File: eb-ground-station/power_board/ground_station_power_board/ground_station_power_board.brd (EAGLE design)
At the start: 125 x 78 mm, 70 parts, among them J1 CONN_20X2SHROUDED, Q1 SQJ459EP_MOSFET_P_CHAN, Q15 DMN61D8LVT-DUAL-N-CHANNEL-MOS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, Q17 DMN61D8LVT-DUAL-N-CHANNEL-MOS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, Q18 DMN61D8LVT-DUAL-N-CHANNEL-MOS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, Q2 SQJ459EP_MOSFET_P_CHAN, Q22 TC4427-FET-GATE-DRVR, Q23 TC4427-FET-GATE-DRVR, Q24 TC4427-FET-GATE-DRVR, Q3 SQJ459EP_MOSFET_P_CHAN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

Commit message: every time I look at this I add 40 more vias
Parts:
- added J2: (no value), SparkFun-Connectors:1X01NS_KIT
- added R14: 4.7k, SparkFun-Resistors:0603
- added U$8: (no value), Oliver_Custom:PSAS_LOGO_15X15
- R10, R8, R9: value EXB-A10P391JC_ARRAY_EXBA-M -> 10k
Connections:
- new net N$6: J2.1, R14.1, U2.14
- net 3.3V: now also R14.2
- net GND: no longer U2.14
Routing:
- net N$6: track 0.00 -> 13.9 mm, vias 0 -> 2
- net 3.3V: track 106.5 -> 108.6 mm
- net GND: vias 297 -> 314
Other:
- board text added: "!RESET->"
- board text added: "1.5A MAX"
- board text added: "10A MAX"
- board text added: "30A MAX"
- board text added: "500mA MAX"
- board text added: "ORESAT GROUND STATION POWER BOARD OLIVER REW 2018-07-31"
- board text removed: "ORESAT GROUND STATION POWER BOARD OLIVER REW 2018-07-29"

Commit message: added decoupling cap and some labels
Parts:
- added C11: 0.1uF, SparkFun-Capacitors:0603
- moved D5 3.00 mm to (12.9, 62.1)
- moved R3 3.00 mm to (12.9, 60.0)
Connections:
- net 3.3V: now also C11.1
- net GND: now also C11.2
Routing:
- net 3.3V: track 108.6 -> 109.9 mm
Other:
- board text added: "LOWER"
- board text added: "UPPER"
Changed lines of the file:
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@@
 <layer number="22" name="bPlace" color="7" fill="1" visible="yes" active="yes"/>
 <layer number="23" name="tOrigins" color="15" fill="1" visible="yes" active="yes"/>
-<layer number="24" name="bOrigins" color="15" fill="1" visible="yes" active="yes"/>
+<layer number="24" name="bOrigins" color="15" fill="1" visible="no" active="yes"/>
 <layer number="25" name="tNames" color="7" fill="1" visible="yes" active="yes"/>
 <layer number="26" name="bNames" color="7" fill="1" visible="yes" active="yes"/>
@@
 <text x="73" y="75" size="1.2" layer="21" ratio="15" rot="SR0">ADC-IN</text>
 <text x="75" y="57" size="1.2" layer="21" ratio="15" rot="SR0">GROUND</text>
-<wire x1="23.36" y1="61.05" x2="18.36" y2="61.05" width="0.5" layer="21"/>
-<wire x1="18.36" y1="61.05" x2="13.36" y2="61.05" width="0.5" layer="21"/>
-<wire x1="13.36" y1="61.05" x2="13.36" y2="66.05" width="0.5" layer="21"/>
-<wire x1="13.36" y1="66.05" x2="18.36" y2="66.05" width="0.5" layer="21"/>
-<wire x1="18.36" y1="66.05" x2="23.36" y2="66.05" width="0.5" layer="21"/>
-<wire x1="23.36" y1="66.05" x2="23.36" y2="61.05" width="0.5" layer="21"/>
-<wire x1="18.36" y1="66.05" x2="18.36" y2="61.05" width="0.5" layer="21"/>
-<text x="14.09" y="62.775" size="1.5" layer="21" ratio="15" rot="SR0">12V</text>
-<text x="18.945" y="62.775" size="1.5" layer="21" ratio="15" rot="SR0">GND</text>
+<wire x1="20.36" y1="61.05" x2="15.36" y2="61.05" width="0.5" layer="21"/>
+<wire x1="15.36" y1="61.05" x2="10.36" y2="61.05" width="0.5" layer="21"/>
+<wire x1="10.36" y1="61.05" x2="10.36" y2="66.05" width="0.5" layer="21"/>
+<wire x1="10.36" y1="66.05" x2="15.36" y2="66.05" width="0.5" layer="21"/>
+<wire x1="15.36" y1="66.05" x2="20.36" y2="66.05" width="0.5" layer="21"/>
+<wire x1="20.36" y1="66.05" x2="20.36" y2="61.05" width="0.5" layer="21"/>
+<wire x1="15.36" y1="66.05" x2="15.36" y2="61.05" width="0.5" layer="21"/>
+<text x="11.09" y="62.775" size="1.5" layer="21" ratio="15" rot="SR0">12V</text>
+<text x="15.945" y="62.775" size="1.5" layer="21" ratio="15" rot="SR0">GND</text>
 <text x="24.5" y="70.75" size="0.8128" layer="21" ratio="15" rot="SR0">A1</text>
 <text x="29.5" y="70.75" size="0.8128" layer="21" ratio="15" rot="SR0">A0</text>
@@
 <text x="55.375" y="72.75" size="1" layer="21" ratio="15" rot="SR0">500mA MAX</text>
 <text x="38.25" y="59.125" size="1" layer="21" ratio="15" rot="SR0">1.5A MAX</text>
-<text x="15.5" y="66.625" size="1" layer="21" ratio="15" rot="SR0">30A MAX</text>
+<text x="12.5" y="66.625" size="1" layer="21" ratio="15" rot="SR0">30A MAX</text>
 <text x="58.375" y="59.25" size="1" layer="21" ratio="15" rot="SR0">500mA MAX</text>
+<text x="26.375" y="61.25" size="1" layer="21" ratio="15" rot="SR90">LOWER</text>
+<text x="23.375" y="67.25" size="1" layer="21" ratio="15" rot="SR90">UPPER</text>
 </plain>
 <attributes>
@@
 <attribute name="VALUE" x="39.5" y="62.635" size="0.6096" layer="27" font="vector" ratio="20" rot="R180" align="top-center"/>
 </element>
-<element name="D5" library="SparkFun-LED" package="LED-0603" value="" x="15.86" y="62.065" smashed="yes">
-<attribute name="NAME" x="12.485" y="62.305" size="0.6096" layer="25" font="vector" ratio="15" rot="R180" align="bottom-center"/>
-<attribute name="VALUE" x="15.86" y="61.43" size="0.6096" layer="27" font="vector" ratio="20" align="top-center"/>
-</element>
-<element name="R3" library="SparkFun-Resistors" package="0603" value="806" x="15.89" y="59.995" smashed="yes" rot="R180">
-<attribute name="NAME" x="13.515" y="60.233" size="0.6096" layer="25" font="vector" ratio="15" rot="R180" align="bottom-center"/>
-<attribute name="PROD_ID" value="RES-07857" x="15.89" y="59.995" size="1.778" layer="27" rot="R180" display="off"/>
-<attribute name="VALUE" x="15.89" y="60.757" size="0.6096" layer="27" font="vector" ratio="20" rot="R180" align="top-center"/>
+<element name="D5" library="SparkFun-LED" package="LED-0603" value="" x="12.86" y="62.065" smashed="yes">
+<attribute name="NAME" x="9.485" y="62.305" size="0.6096" layer="25" font="vector" ratio="15" rot="R180" align="bottom-center"/>
+<attribute name="VALUE" x="12.86" y="61.43" size="0.6096" layer="27" font="vector" ratio="20" align="top-center"/>
+</element>
+<element name="R3" library="SparkFun-Resistors" package="0603" value="806" x="12.89" y="59.995" smashed="yes" rot="R180">
+<attribute name="NAME" x="10.515" y="60.233" size="0.6096" layer="25" font="vector" ratio="15" rot="R180" align="bottom-center"/>
+<attribute name="PROD_ID" value="RES-07857" x="12.89" y="59.995" size="1.778" layer="27" rot="R180" display="off"/>
+<attribute name="VALUE" x="12.89" y="60.757" size="0.6096" layer="27" font="vector" ratio="20" rot="R180" align="top-center"/>
 </element>
 <element name="D6" library="SparkFun-LED" package="LED-0603" value="" x="34.5" y="62" smashed="yes" rot="R180">
@@
 </element>
 <element name="U$8" library="Oliver_Custom" package="PSAS_LOGO_15X15" value="" x="26.5" y="54" rot="MR0"/>
+<element name="C11" library="SparkFun-Capacitors" package="0603" value="0.1uF" x="112.375" y="6">
+<attribute name="PROD_ID" value="CAP-08604" x="112.375" y="6" size="1.778" layer="27" display="off"/>
+</element>
 </elements>
 <signals>
@@
 <via x="113" y="32" extent="1-16" drill="0.254"/>
 <via x="114" y="37" extent="1-16" drill="0.254"/>
-<via x="114" y="11" extent="1-16" drill="0.254"/>
-<via x="112" y="11" extent="1-16" drill="0.254"/>
-<via x="115" y="6" extent="1-16" drill="0.254"/>
-<via x="113" y="6" extent="1-16" drill="0.254"/>
-<via x="111" y="6" extent="1-16" drill="0.254"/>
+<via x="114" y="15.5" extent="1-16" drill="0.254"/>
+<via x="112" y="15.5" extent="1-16" drill="0.254"/>
+<via x="114.5" y="6" extent="1-16" drill="0.254"/>
+<via x="113.5" y="4.5" extent="1-16" drill="0.254"/>
+<via x="111" y="4.5" extent="1-16" drill="0.254"/>
 <via x="111" y="1" extent="1-16" drill="0.254"/>
 <via x="115" y="1" extent="1-16" drill="0.254"/>
@@
 <via x="34" y="5" extent="1-16" drill="0.254"/>
 <via x="9" y="68" extent="1-16" drill="0.254"/>
-<via x="8" y="63" extent="1-16" drill="0.254"/>
+<via x="12" y="65" extent="1-16" drill="0.254"/>
 <via x="9" y="58" extent="1-16" drill="0.254"/>
 <via x="10" y="71" extent="1-16" drill="0.254"/>
@@
 <via x="20" y="71" extent="1-16" drill="0.254"/>
 <via x="28" y="71" extent="1-16" drill="0.254"/>
-<via x="23.125" y="68.5" extent="1-16" drill="0.254"/>
+<via x="21.625" y="70" extent="1-16" drill="0.254"/>
 <via x="98" y="72" extent="1-16" drill="0.254"/>
 <via x="90.5" y="55" extent="1-16" drill="0.254"/>
@@
 <via x="43.5" y="58" extent="1-16" drill="0.254"/>
 <via x="38.5" y="58" extent="1-16" drill="0.254"/>
-<via x="25" y="63.5" extent="1-16" drill="0.254"/>
+<via x="25" y="61" extent="1-16" drill="0.254"/>
 <via x="1.5" y="55" extent="1-16" drill="0.254"/>
 <via x="63" y="37" extent="1-16" drill="0.254"/>
@@
 <via x="27" y="22.5" extent="1-16" drill="0.254"/>
 <via x="67" y="56" extent="1-16" drill="0.254"/>
-<via x="17.125" y="65.125" extent="1-16" drill="0.254"/>
+<via x="21.625" y="62.625" extent="1-16" drill="0.254"/>
+<contactref element="C11" pad="2"/>
 </signal>
 <signal name="OUT16">
@@
 <contactref element="Q6" pad="S1"/>
 <contactref element="Q6" pad="S2"/>
-<wire x1="14.983" y1="62.065" x2="14.395" y2="62.065" width="0.4" layer="1"/>
-<wire x1="14.395" y1="62.065" x2="13.74" y2="61.41" width="0.4" layer="1"/>
-<wire x1="13.74" y1="61.41" x2="13.74" y2="54.26" width="0.4" layer="1"/>
+<wire x1="11.983" y1="62.065" x2="11.395" y2="62.065" width="0.4" layer="1"/>
+<wire x1="11.395" y1="62.065" x2="10.74" y2="61.41" width="0.4" layer="1"/>
+<wire x1="10.74" y1="61.41" x2="10.74" y2="54.26" width="0.4" layer="1"/>
 </signal>
 <signal name="3.3V">
@@
 <wire x1="104.5" y1="56.85" x2="104.5" y2="58.86020625" width="0.2" layer="1"/>
 <wire x1="104.5" y1="58.86020625" x2="104.430103125" y2="58.930103125" width="0.2" layer="1"/>
+<contactref element="C11" pad="1"/>
+<wire x1="111.525" y1="6" x2="111.525" y2="7.2228" width="0.35" layer="1"/>
+<wire x1="111.525" y1="7.2228" x2="111.5522" y2="7.25" width="0.35" layer="1"/>
 </signal>
 <signal name="SDA">
@@
 <contactref element="D5" pad="C"/>
 <contactref element="R3" pad="1"/>
-<wire x1="16.737" y1="62.065" x2="16.74" y2="62.062" width="0.4" layer="1"/>
-<wire x1="16.74" y1="62.062" x2="16.74" y2="59.995" width="0.4" layer="1"/>
+<wire x1="13.737" y1="62.065" x2="13.74" y2="62.062" width="0.4" layer="1"/>
+<wire x1="13.74" y1="62.062" x2="13.74" y2="59.995" width="0.4" layer="1"/>
 </signal>
 <signal name="N$14">

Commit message: added SMPS
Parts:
- removed C3, C4: 10uF, SparkFun-Capacitors:0805
- removed C5: 0.1uF, SparkFun-Capacitors:0603
- removed U3: MIC5239-3.3YMMMSOP-8_MM-M, GROUND-STATION-POWER-BOARD:MSOP-8_MM-M
- added C12: 10uF, SparkFun-Capacitors:1206
- added C13: 22UF-1210-16V-20%, SparkFun-Capacitors:1210
- added TP1: TEST-POINT3, SparkFun-Connectors:PAD.03X.03
- added U$9: LMZM23601V3SILT, GROUND-STATION-POWER-BOARD:MICRO-SIP
- moved C7 16.3 mm to (110.0, 43.5), turned to 0 degrees
- moved C6 2.50 mm to (101.3, 33.6)
- moved E1 2.50 mm to (97.4, 36.2)
- moved E2 2.50 mm to (95.3, 36.2)
- moved Q23 2.50 mm to (80.2, 41.3)
- moved U1 2.50 mm to (96.4, 32.5)
- moved C9 2.00 mm to (77.2, 41.3)
- moved Q22 1.50 mm to (74.2, 41.3)
- moved C8 1.00 mm to (71.2, 41.3)
- moved Q24 0.50 mm to (68.2, 41.3)
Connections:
- new net N$7: TP1.P$1, U$9.5
- net 12V: now also C12.1, U$9.2, U$9.3, U$9.4; no longer C4.1, U3.1, U3.3
- net 3.3V: now also C13.1, U$9.6, U$9.7; no longer C3.1, C5.1, U3.4
- net GND: now also C12.2, C13.2, U$9.1, U$9.TP, U$9.V1, U$9.V2, U$9.V3; no longer C3.2, C4.2, C5.2, U3.5, U3.6, U3.7, U3.8
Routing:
- net 12V: track 55.8 -> 49.5 mm
- net 3.3V: track 109.9 -> 106.2 mm
- net N$7: track 0.00 -> 3.41 mm
- net SDA: track 103.4 -> 100.9 mm
- net OUT4: track 52.6 -> 55.1 mm
- net OUT3: track 54.0 -> 56.5 mm
- net SCL: track 95.7 -> 93.2 mm
- net HIGH_OUT_4: track 53.0 -> 50.5 mm
- net HIGH_OUT_3: track 56.0 -> 53.5 mm
- net ADC4: track 9.72 -> 12.2 mm
- net OUT6: track 58.3 -> 59.8 mm
- net HIGH_OUT_6: track 58.5 -> 57.0 mm
- net HIGH_OUT_5: track 61.5 -> 60.0 mm
- net OUT5: track 59.9 -> 61.4 mm
- net ADC1: track 9.75 -> 8.57 mm
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- added copper zone on layer 1, net 3.3V
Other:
- board text added: "TP1"

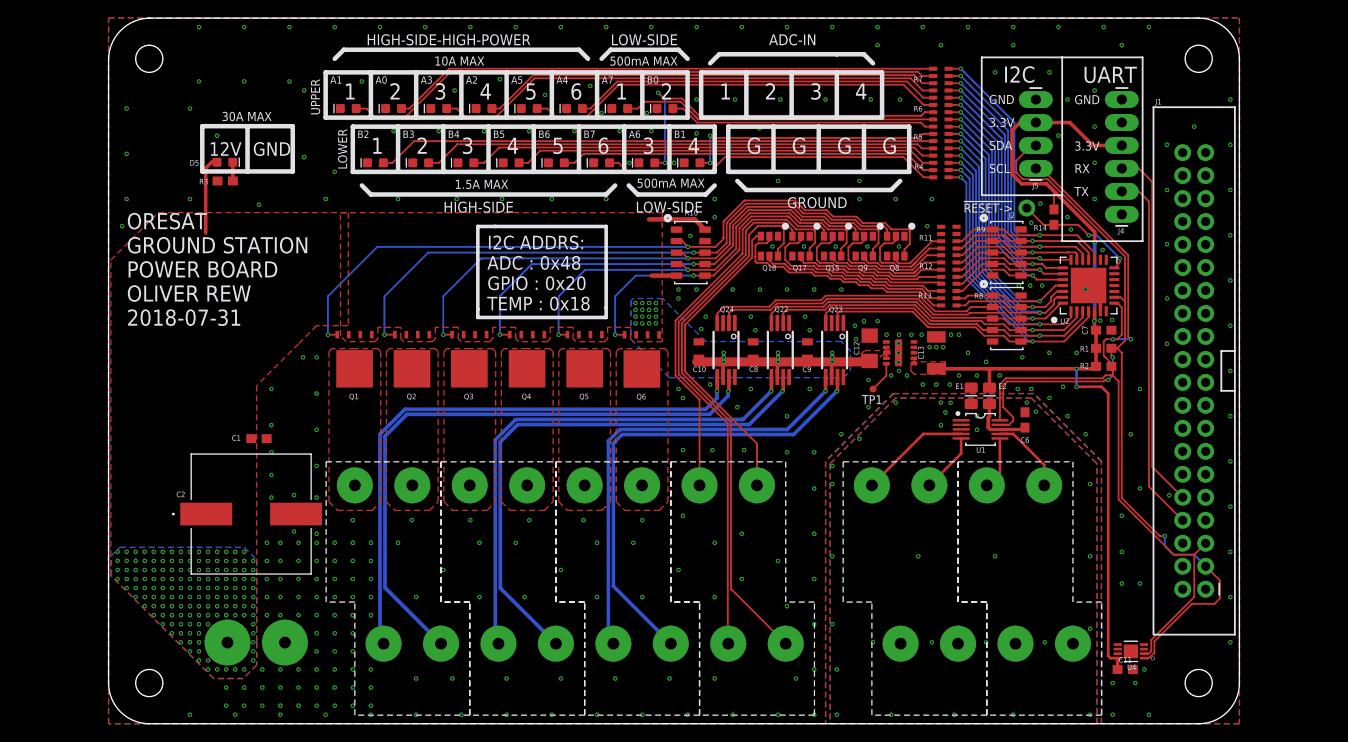
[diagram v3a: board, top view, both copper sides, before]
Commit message: Updated for 2  5V mosfets
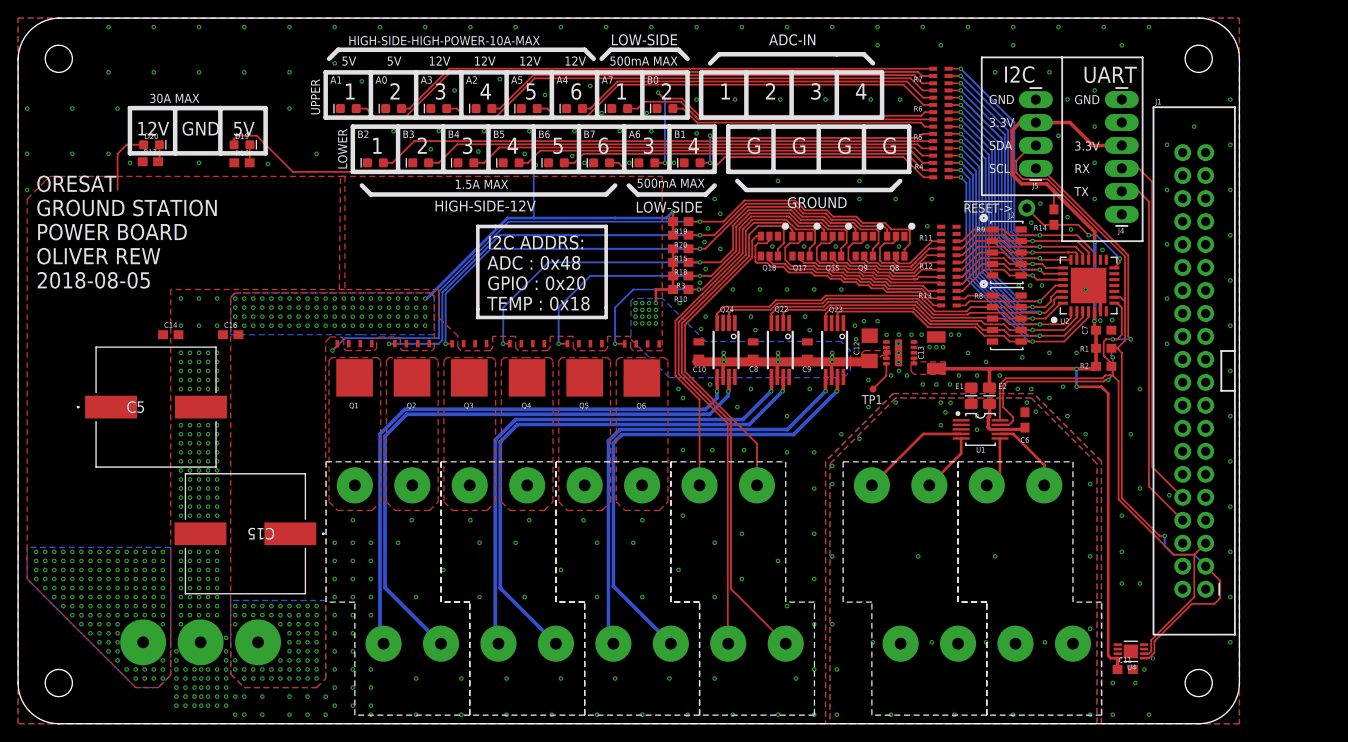
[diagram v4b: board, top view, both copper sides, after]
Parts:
- removed C1: 0.1uF, SparkFun-Capacitors:0603
- removed C2: 100UF, GROUND-STATION-POWER-BOARD:CHEMI-KE0-M
- removed D5: (no value), SparkFun-LED:LED-0603
- removed U$7: 1714955-PHONEIX-CONTACT-TERMINAL-BLOCK, GROUND-STATION-POWER-BOARD:1714955-PHONEIX-CONTACT-TERMINAL-BLOCK
- added C14, C16: 0.1uF, SparkFun-Capacitors:0603
- added C15, C5: 100UF, GROUND-STATION-POWER-BOARD:CHEMI-KE0-M
- added D19, D20: (no value), SparkFun-LED:LED-0603
- added R15, R18, R19, R20: 10k, SparkFun-Resistors:0603
- added R16: 620, SparkFun-Resistors:0603
- added R17: 1500, SparkFun-Resistors:0603
- added U$11: 1714968-PHONEIX-CONTACT-TERMINAL-BLOCK, GROUND-STATION-POWER-BOARD:1714968-PHONEIX-CONTACT-3-TERMINAL-BLOCK
- R10: device temp-lib:C_ARRAY_EXBA-M -> SparkFun-Resistors:0603
- R3: value 806 -> 10k
- moved R3 51.4 mm to (63.2, 49.5)
- moved U$8 40.2 mm to (-13.5, 50.0)
- moved R10 4.22 mm to (63.2, 48.0), turned to 180 degrees
- moved Q1 1.00 mm to (27.2, 39.3)
- moved Q2 1.00 mm to (33.5, 39.3)
- moved Q3 1.00 mm to (39.9, 39.3)
- moved Q4 1.00 mm to (46.3, 39.3)
- moved Q5 1.00 mm to (52.6, 39.3)
- moved Q6 1.00 mm to (59.0, 39.3)
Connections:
- removed net N$9: D5.C, R3.1
- new net +5V: C15.1, C16.2, D19.A, Q1.S1, Q1.S2, Q1.S3, Q2.S1, Q2.S2, Q2.S3, R19.2, R20.2, U$11.3
- new net N$12: D19.C, R16.2
- new net N$18: D20.C, R17.2
- net 12V: now also C14.1, C5.1, D20.A, R10.2, R15.2, R18.2, R3.2, U$11.1; no longer C1.1, C2.1, D5.A, Q1.S1, Q1.S2, Q1.S3, Q2.S1, Q2.S2, Q2.S3, R10.10, R10.5, U$7.1
- net GND: now also C14.2, C15.2, C16.1, C5.2, R16.1, R17.1, U$11.2; no longer C1.2, C2.2, R3.2, U$7.2
- net PWR_FET_G1: now also R20.1; no longer R10.8
- net PWR_FET_G2: now also R19.1; no longer R10.2
- net PWR_FET_G3: now also R18.1; no longer R10.7
- net PWR_FET_G4: now also R15.1; no longer R10.3
- net PWR_FET_G5: now also R10.1; no longer R10.6
- net PWR_FET_G6: now also R3.1; no longer R10.4
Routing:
- net +5V: track 0.00 -> 76.1 mm, vias 0 -> 153
- net 12V: track 49.5 -> 46.6 mm, vias 169 -> 161
- net N$9: track 2.07 -> 0.00 mm
- net N$12: track 0.00 -> 2.01 mm
- net N$18: track 0.00 -> 1.94 mm
- net PWR_FET_G5: track 34.9 -> 36.3 mm
- net PWR_FET_G3: track 51.6 -> 52.6 mm
- net PWR_FET_G4: track 64.4 -> 63.5 mm
- net PWR_FET_G2: track 81.1 -> 80.4 mm
- net GND: vias 331 -> 461
- added copper zone on layer 1, net +5V
- added copper zone on layer 16, net +5V
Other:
- board size 125 x 78 mm -> 135 x 78 mm
- board text added: "5V"
- board text added: "HIGH-SIDE-12V"
- board text added: "HIGH-SIDE-HIGH-POWER-10A-MAX"
- board text added: "ORESAT GROUND STATION POWER BOARD OLIVER REW 2018-08-05"
- board text removed: "10A MAX"
- board text removed: "HIGH-SIDE"
- board text removed: "HIGH-SIDE-HIGH-POWER"
- board text removed: "ORESAT GROUND STATION POWER BOARD OLIVER REW 2018-07-31"

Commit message: small fixes
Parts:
- moved U$8 34.7 mm to (20.5, 43.0)
- moved C10 10.0 mm to (75.2, 41.3)
- moved C11 10.0 mm to (122.4, 6.00)
- moved C12 10.0 mm to (94.1, 41.5)
- moved C13 10.0 mm to (101.5, 41.0)
- moved C14 10.0 mm to (16.9, 43.0)
- moved C15 10.0 mm to (25.1, 21.0)
- moved C16 10.0 mm to (23.5, 43.0)
- moved C5 10.0 mm to (15.2, 35.0)
- moved C6 10.0 mm to (111.3, 33.6)
- moved C7 10.0 mm to (120.0, 43.5)
- moved C8 10.0 mm to (81.2, 41.3)
- moved C9 10.0 mm to (87.2, 41.3)
- moved D1 10.0 mm to (64.5, 62.0)
- moved D10 10.0 mm to (66.5, 68.0)
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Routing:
- net G2: track 12.6 -> 11.8 mm
- net SDA: track 100.9 -> 100.3 mm
- net GND: vias 461 -> 477
